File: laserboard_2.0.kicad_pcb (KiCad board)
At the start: 2 copper layers, 224.9 x 224.9 mm, 212 parts, among them J1 5v, J3 Serial Com, J4 Serial Com to rasberry, Q1 IRLML6401, Q10 IRLML6401, Q11 IRLML6401, Q12 IRLML6401, Q13 IRLML6401, Q14 IRLML6401, Q15 IRLML6401, Q16 IRLML6401, Q17 IRLML6401, Q18 IRLML6401, Q19 IRLML6401, Q2 IRLML6401, Q20 IRLML6401, Q21 IRLML6401, Q22 IRLML6401, Q23 IRLML6401, Q24 IRLML6401, Q25 IRLML6401, Q26 IRLML6401, Q27 IRLML6401, Q28 IRLML6401, Q29 IRLML6401, Q3 IRLML6401, Q30 IRLML6401, Q31 IRLML6401, Q32 IRLML6401, Q33 IRLML6401, Q34 IRLML6401, Q35 IRLML6401, Q36 IRLML6401, Q37 IRLML6401, Q38 IRLML6401, Q39 IRLML6401, Q4 IRLML6401, Q40 IRLML6401, Q41 IRLML6401, Q42 IRLML6401, Q43 IRLML6401, Q44 IRLML6401, Q45 IRLML6401, Q46 IRLML6401, Q47 IRLML6401, Q48 IRLML6401, Q49 IRLML6401, Q5 IRLML6401, Q50 IRLML6401, Q6 IRLML6401, Q7 IRLML6401, Q8 IRLML6401, Q9 IRLML6401, U1 Teensy4.1, U2 MCP23017_ML

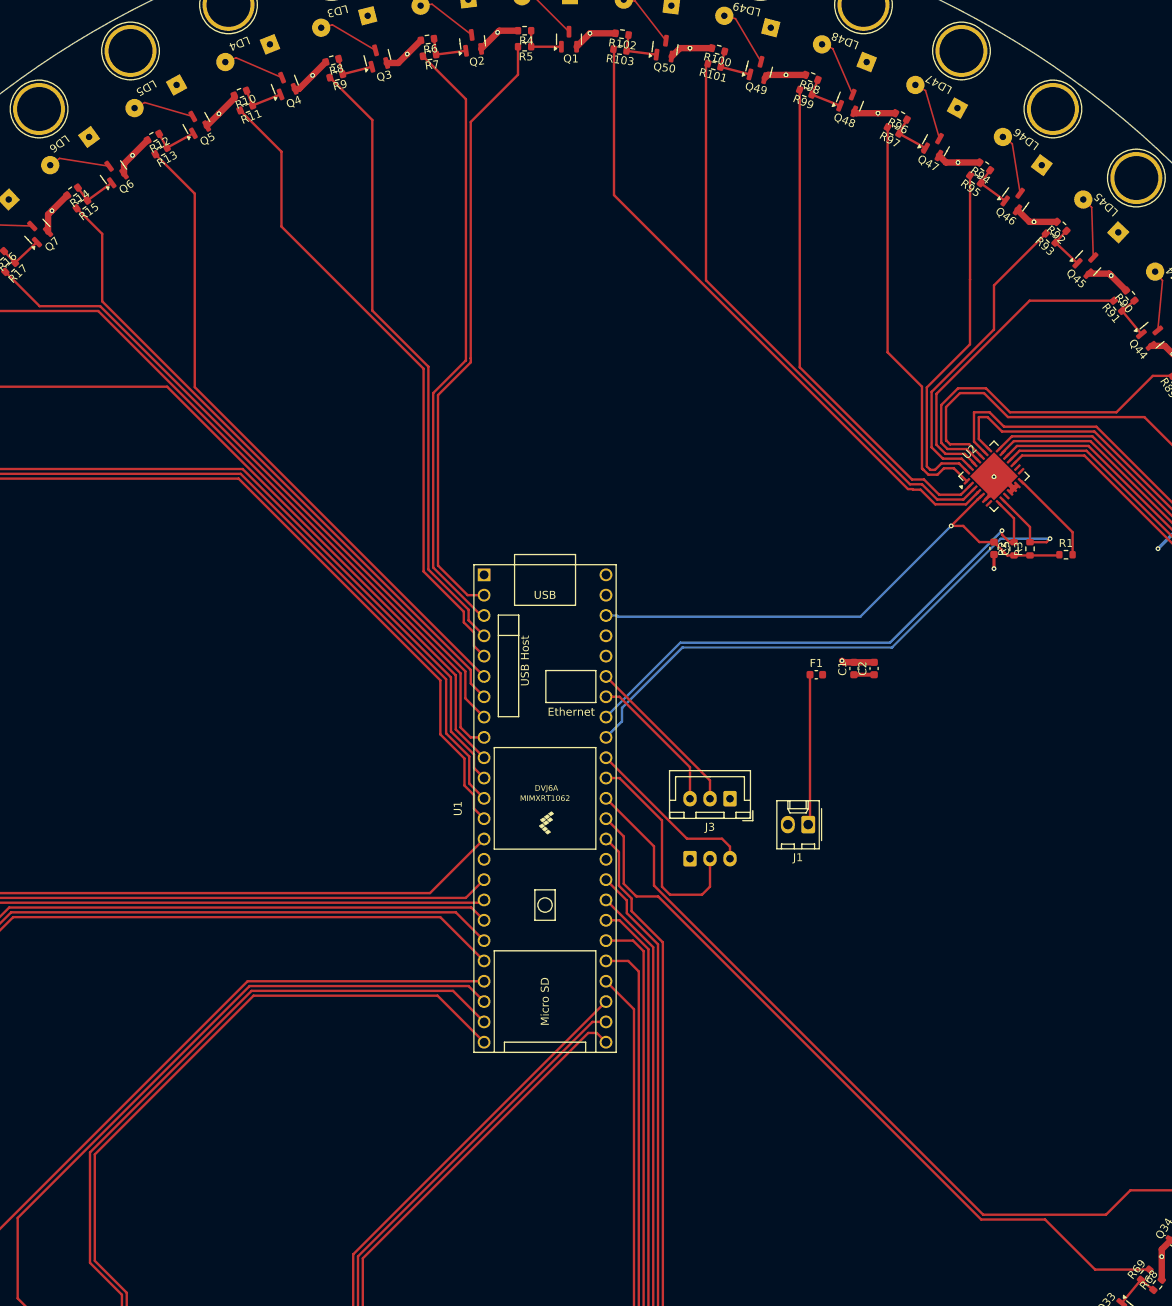
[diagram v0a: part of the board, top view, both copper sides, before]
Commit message: Finalize
- Copper fills
- Trees
- Holes
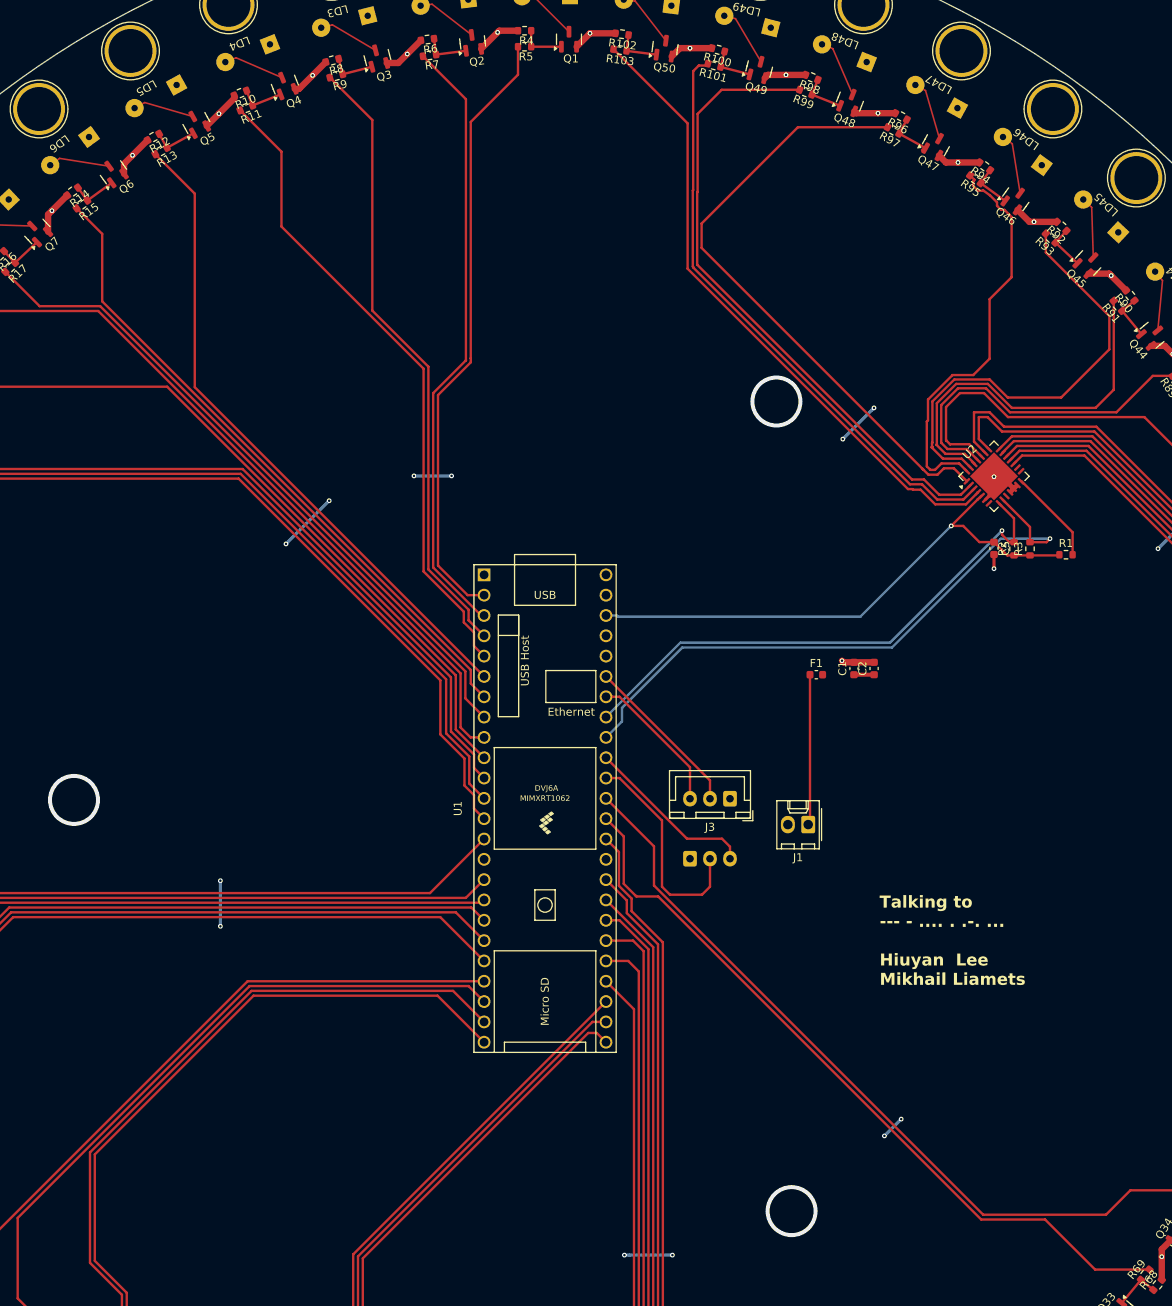
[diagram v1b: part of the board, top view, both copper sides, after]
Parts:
- added G***: LOGO, LOGO, B.Cu at (198.8, 245.2)
- added G***: LOGO, LOGO, B.Cu at (198.9, 94.7)
- added G***: LOGO, LOGO, B.Cu at (199.3, 160.1)
- added G***: LOGO, LOGO, B.Cu at (199.2, 9.70)
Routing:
- net Laser power: track 22.5 -> 55.1 mm, vias 1 -> 13
- net /A47: track 51.6 -> 77.4 mm
- net /A45: track 38.6 -> 56.3 mm
- net /A48: track 63.1 -> 79.5 mm
- net /A44: track 39.1 -> 47.5 mm
- net /A46: track 44.5 -> 51.2 mm
- net /A49: track 72.6 -> 74.5 mm
- net (no net): vias 0 -> 3
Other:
- board text added: "Talking to --- - .... . .-. ... Hiuyan Lee Mikhail Liamets"
